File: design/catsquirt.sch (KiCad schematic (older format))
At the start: 27 parts, among them P1 CONN_8X2_CATSQUIRT, P2 BDM, P3 CONN_2, P4 CONN_8X2_CATSQUIRT, P5 CONN_8X2_CATSQUIRT, SW1 SW_PUSH, U1 MC9S12XDP512, X1 CRYSTAL

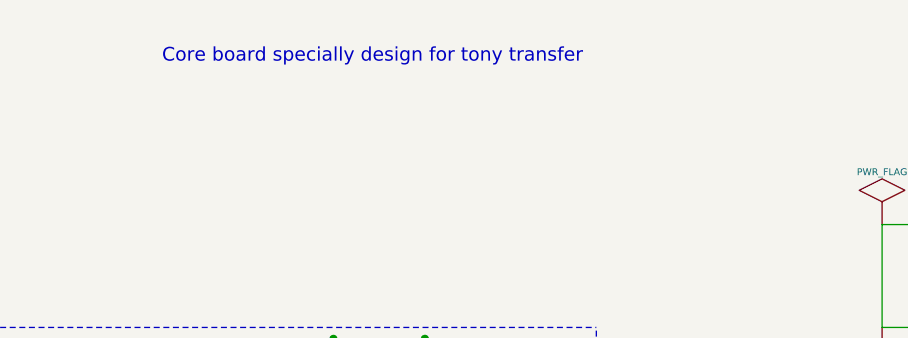
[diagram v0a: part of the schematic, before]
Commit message: Dan's style schema in KiCAD first uploaded
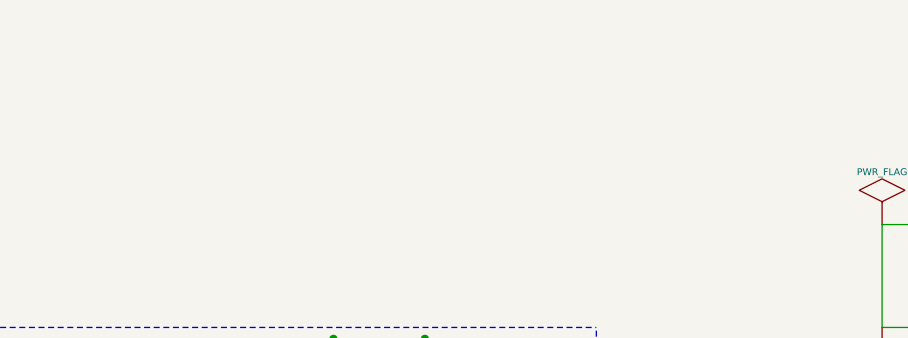
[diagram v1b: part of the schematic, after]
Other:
- note removed: "Core board specially design for tony transfer"
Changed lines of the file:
@@
-EESchema Schematic File Version 2  date 03/10/2011 22:36:14
+EESchema Schematic File Version 2  date 10/10/2011 12:09:13
 LIBS:power
 LIBS:device
@@
 Sheet 1 1
 Title ""
-Date "22 sep 2011"
+Date "10 oct 2011"
 Rev "v0.01"
 Comp "diyefi.org"
@@
 	1    0    0    -1
 $EndComp
-Text Notes 4350 1950 0    60   ~ 0
-Core board specially design for tony transfer
 NoConn ~ 10750 6850
 NoConn ~ 10750 6650
